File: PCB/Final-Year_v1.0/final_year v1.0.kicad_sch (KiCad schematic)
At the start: 37 parts, among them J1 Power In, J2 Screw_Terminal_01x07, J3 Screw_Terminal_01x03, J4 Screw_Terminal_01x04, J5 Screw_Terminal_01x03, J6 PT1000, J7 HCPV 22x, J8 LDR_module, J9 Screw_Terminal_01x03, U1 LM7805_TO220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

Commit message: added libraries
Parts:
- added BZ1: Buzzer, Buzzer:Buzzer_12x9.5RM7.6, symbol Device:Buzzer
- added C6: 100nF, Capacitor_THT:C_Disc_D6.0mm_W2.5mm_P5.00mm, symbol Device:C
- added C7: 10nF, Capacitor_SMD_2:C_0201_0603Metric, symbol Device:C
- added C8: 0.1uF, Capacitor_THT:C_Disc_D6.0mm_W2.5mm_P5.00mm, symbol Device:C
- added D1: CQY99, LED_THT:LED_D5.0mm_IRGrey, symbol LED:CQY99
- added Q1: 2N3904, Package_TO_SOT_THT:TO-92_Inline, symbol Transistor_BJT:2N3904
- added R19: 1k, Resistor_SMD:R_0201_0603Metric, symbol Device:R
- added R20: 1.2k, Resistor_SMD:R_0201_0603Metric, symbol Device:R
- C1, C4, C5: footprint (none) -> Capacitor_THT:C_Disc_D6.0mm_W2.5mm_P5.00mm
- C2, C3: footprint (none) -> Capacitor_SMD_2:C_0201_0603Metric
- J1, J6: footprint (none) -> TerminalBlock_Phoenix:TerminalBlock_Phoenix_MKDS-1,5-2-5.08_1x02_P5.08mm_Horizontal
- J2: footprint (none) -> TerminalBlock_Phoenix:TerminalBlock_Phoenix_MKDS-1,5-7-5.08_1x07_P5.08mm_Horizontal
- J3, J5, J7, J8, J9: footprint (none) -> TerminalBlock_Phoenix:TerminalBlock_Phoenix_MKDS-1,5-3-5.08_1x03_P5.08mm_Horizontal
- J4: footprint (none) -> TerminalBlock_Phoenix:TerminalBlock_Phoenix_MKDS-1,5-4-5.08_1x04_P5.08mm_Horizontal
- R1, R14, R15, R16, R17, R18, R2, R3: footprint (none) -> Resistor_SMD:R_0201_0603Metric
- R10, R11, R12, R13, R4, R5, R6, R7, R8, R9: footprint (none) -> Resistor_THT:R_Axial_DIN0207_L6.3mm_D2.5mm_P10.16mm_Horizontal
- U5: footprint (none) -> Package_DIP:DIP-14_W7.62mm
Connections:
- net +12V: now also BZ1.1 (-)
- net GND: now also C6.1, C7.1, C8.1, D1.1 (K), Q1.1 (E)
- net at J6.2 (Pin_2), R10.2, U5.5 (+): now also C6.2
- net at R7.2, R8.1, U5.3 (+): now also C7.2
- net D33: now reaches U4.22 (D33)
- net D33: now also R20.1
- net D12: now reaches U4.27 (D12)
- net D12: now also R19.1
- net at R16.2, R17.1, U5.12 (+): now also C8.2
- new net: D1.2 (A), R19.2
- new net: BZ1.2 (+), Q1.3 (C)
- new net: Q1.2 (B), R20.2
- no-connect marks 16 -> 14
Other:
- note added: "Buzzer"
- note added: "Converts 0V - 5V to 0V TO 2V readable range"
- note added: "Final year project"
- note added: "LED"
- note added: "power terminals"

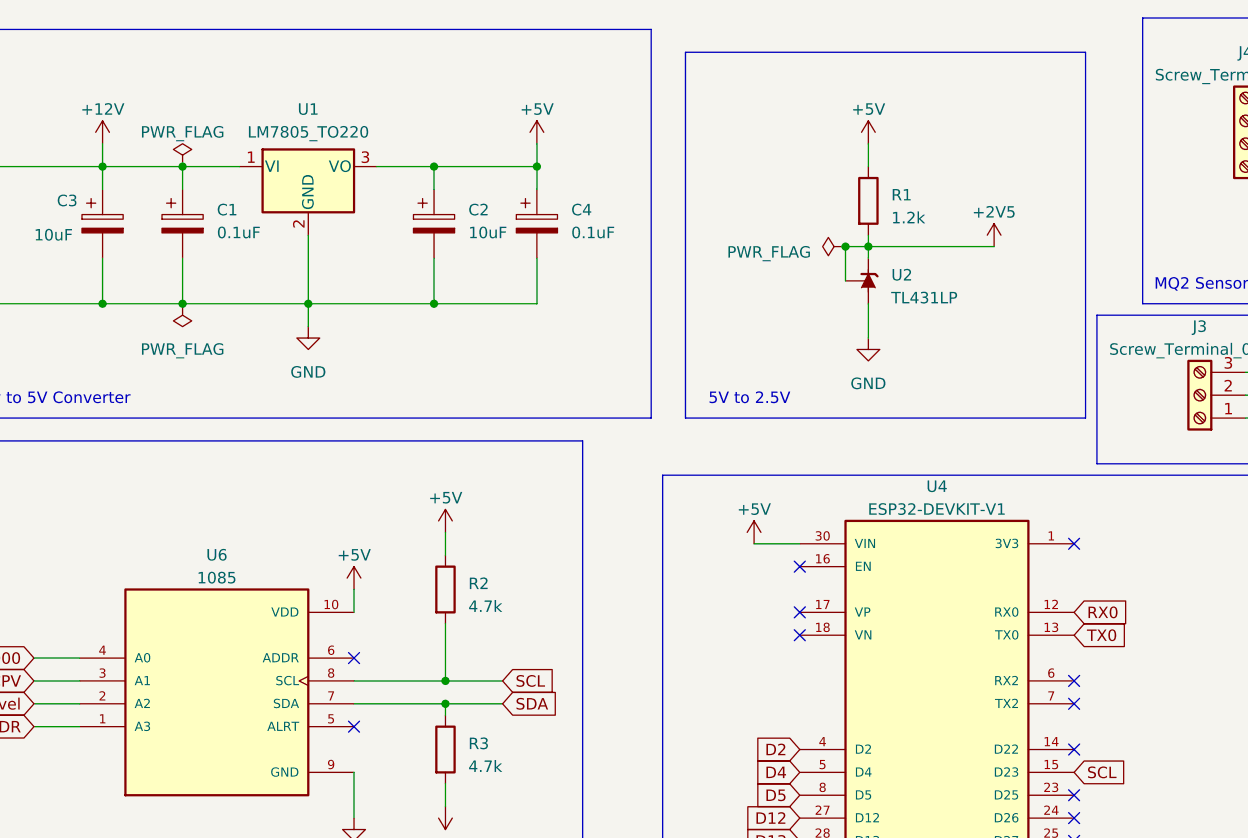
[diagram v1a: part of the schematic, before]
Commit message: address to gnd and decoupling cap to ads
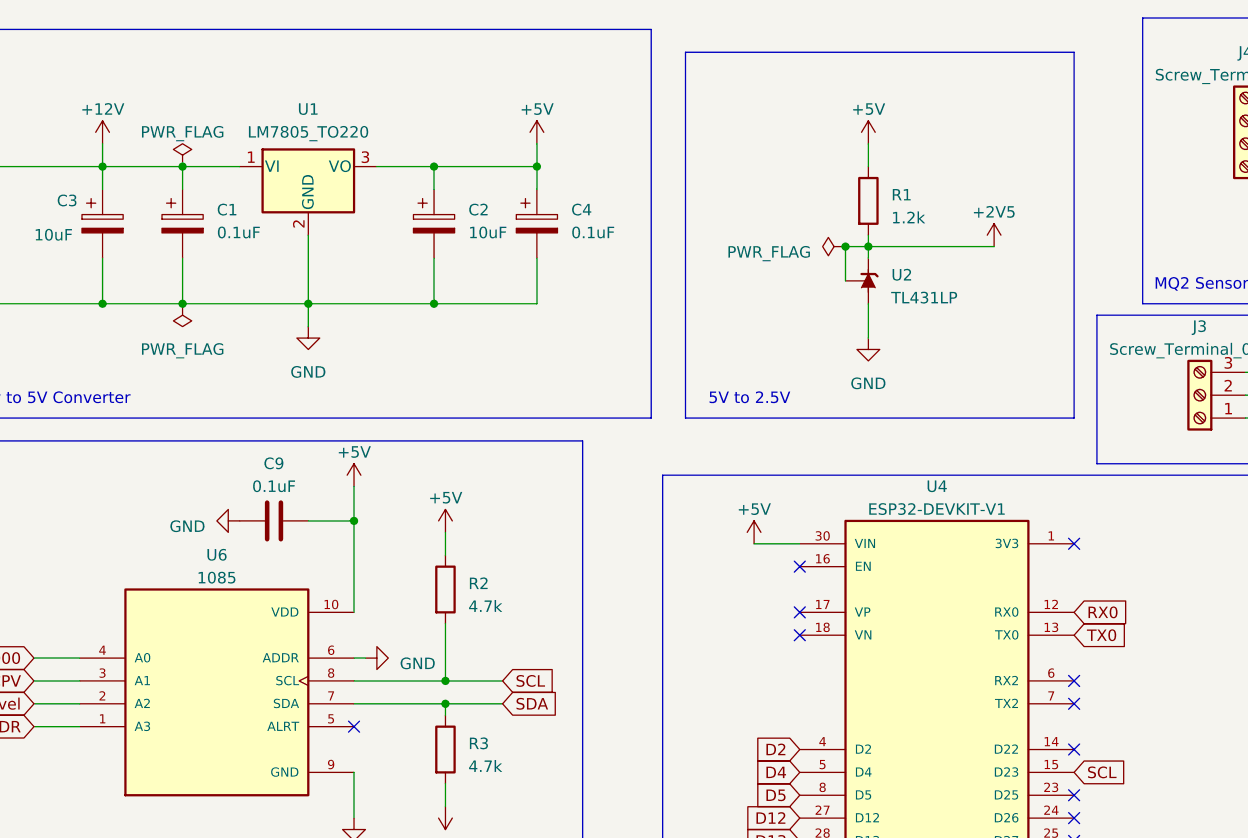
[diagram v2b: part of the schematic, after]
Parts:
- added C9: 0.1uF, Capacitor_THT:C_Disc_D6.0mm_W2.5mm_P5.00mm, symbol Device:C
- BZ1: footprint Buzzer:Buzzer_12x9.5RM7.6 -> Buzzer_Beeper:Buzzer_12x9.5RM7.6
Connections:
- net +5V: now also C9.2
- net GND: now also U6.6 (ADDR), C9.1
- no-connect marks 14 -> 13
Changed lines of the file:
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@@
   (junction (at 43.18 44.45) (diameter 0) (color 0 0 0 0)
+  )
+  (junction (at 71.12 68.58) (diameter 0) (color 0 0 0 0)
   )
   (junction (at 81.28 88.9) (diameter 0) (color 0 0 0 0)
@@
   (no_connect (at 151.13 104.14))
   (no_connect (at 120.65 81.28))
-  (no_connect (at 71.12 83.82))
   (no_connect (at 151.13 111.76))
   (no_connect (at 151.13 88.9))
@@
     (stroke (width 0) (type default))
   )
+  (wire (pts (xy 71.12 68.58) (xy 71.12 78.74))
+    (stroke (width 0) (type default))
+  )
   (wire (pts (xy 240.03 87.63) (xy 220.98 87.63))
     (stroke (width 0) (type default))
@@
     (stroke (width 0) (type default))
   )
+  (wire (pts (xy 66.04 68.58) (xy 71.12 68.58))
+    (stroke (width 0) (type default))
+  )
   (wire (pts (xy 106.68 176.53) (xy 114.3 176.53))
     (stroke (width 0) (type default))
@@
     (stroke (width 0) (type default))
   )
+  (wire (pts (xy 71.12 83.82) (xy 72.39 83.82))
+    (stroke (width 0) (type default))
+  )
   (wire (pts (xy 128.27 142.24) (xy 128.27 144.78))
     (stroke (width 0) (type default))
@@
     (stroke (width 0) (type default))
   )
-  (wire (pts (xy 71.12 76.2) (xy 71.12 78.74))
+  (wire (pts (xy 71.12 64.77) (xy 71.12 68.58))
     (stroke (width 0) (type default))
   )
@@
     (fill (type none))
   )
-  (rectangle (start 107.95 16.51) (end 152.4 57.15)
+  (rectangle (start 107.95 16.51) (end 151.13 57.15)
     (stroke (width 0) (type default))
     (fill (type none))
@@
       (effects (font (size 1.27 1.27)) (justify left))
     )
-    (property "Footprint" "Buzzer:Buzzer_12x9.5RM7.6" (at 319.405 31.75 90)
+    (property "Footprint" "Buzzer_Beeper:Buzzer_12x9.5RM7.6" (at 319.405 31.75 90)
       (effects (font (size 1.27 1.27)) hide)
     )
@@
     )
   )
-  (symbol (lib_id "power:+5V") (at 71.12 76.2 0) (unit 1)
-    (in_bom yes) (on_board yes) (dnp no) (fields_autoplaced)
-    (property "Reference" "#PWR07" (at 71.12 80.01 0)
-      (effects (font (size 1.27 1.27)) hide)
-    )
-    (property "Value" "+5V" (at 71.12 72.39 0)
-      (effects (font (size 1.27 1.27)))
-    )
-    (property "Footprint" "" (at 71.12 76.2 0)
-      (effects (font (size 1.27 1.27)) hide)
-    )
-    (property "Datasheet" "" (at 71.12 76.2 0)
+  (symbol (lib_id "power:+5V") (at 71.12 64.77 0) (unit 1)
+    (in_bom yes) (on_board yes) (dnp no)
+    (property "Reference" "#PWR07" (at 71.12 68.58 0)
+      (effects (font (size 1.27 1.27)) hide)
+    )
+    (property "Value" "+5V" (at 71.12 60.96 0)
+      (effects (font (size 1.27 1.27)))
+    )
+    (property "Footprint" "" (at 71.12 64.77 0)
+      (effects (font (size 1.27 1.27)) hide)
+    )
+    (property "Datasheet" "" (at 71.12 64.77 0)
       (effects (font (size 1.27 1.27)) hide)
     )
@@
     )
   )
+  (symbol (lib_id "power:GND") (at 72.39 83.82 90) (unit 1)
+    (in_bom yes) (on_board yes) (dnp no) (fields_autoplaced)
+    (property "Reference" "#PWR044" (at 78.74 83.82 0)
+      (effects (font (size 1.27 1.27)) hide)
+    )
+    (property "Value" "GND" (at 76.2 84.455 90)
+      (effects (font (size 1.27 1.27)) (justify right))
+    )
+    (property "Footprint" "" (at 72.39 83.82 0)
+      (effects (font (size 1.27 1.27)) hide)
+    )
+    (property "Datasheet" "" (at 72.39 83.82 0)
+      (effects (font (size 1.27 1.27)) hide)
+    )
+    (pin "1")
+    (instances
+      (project "final_year v1.0"
+        (path "/49226e52-308e-4c85-869a-6307490999e3"
+          (reference "#PWR044") (unit 1)
+        )
+      )
+    )
+  )
   (symbol (lib_id "Connector:Screw_Terminal_01x03") (at 165.1 54.61 180) (unit 1)
     (in_bom yes) (on_board yes) (dnp no)
@@
         (path "/49226e52-308e-4c85-869a-6307490999e3"
           (reference "#PWR027") (unit 1)
+        )
+      )
+    )
+  )
+  (symbol (lib_id "Device:C") (at 62.23 68.58 90) (unit 1)
+    (in_bom yes) (on_board yes) (dnp no) (fields_autoplaced)
+    (property "Reference" "C9" (at 62.23 62.23 90)
+      (effects (font (size 1.27 1.27)))
+    )
+    (property "Value" "0.1uF" (at 62.23 64.77 90)
+      (effects (font (size 1.27 1.27)))
+    )
+    (property "Footprint" "Capacitor_THT:C_Disc_D6.0mm_W2.5mm_P5.00mm" (at 66.04 67.6148 0)
+      (effects (font (size 1.27 1.27)) hide)
+    )
+    (property "Datasheet" "~" (at 62.23 68.58 0)
+      (effects (font (size 1.27 1.27)) hide)
+    )
+    (pin "1")
+    (pin "2")
+    (instances
+      (project "final_year v1.0"
+        (path "/49226e52-308e-4c85-869a-6307490999e3"
+          (reference "C9") (unit 1)
         )
       )
@@
         )
       )
+    )
+  )
+  (symbol (lib_id "power:GND") (at 58.42 68.58 270) (unit 1)
+    (in_bom yes) (on_board yes) (dnp no) (fields_autoplaced)
+    (property "Reference" "#PWR045" (at 52.07 68.58 0)
+      (effects (font (size 1.27 1.27)) hide)
+    )
+    (property "Value" "GND" (at 54.61 69.215 90)
+      (effects (font (size 1.27 1.27)) (justify right))
+    )
+    (property "Footprint" "" (at 58.42 68.58 0)
+      (effects (font (size 1.27 1.27)) hide)
+    )
+    (property "Datasheet" "" (at 58.42 68.58 0)
+      (effects (font (size 1.27 1.27)) hide)
+    )
+    (pin "1")
+    (instances
+      (project "final_year v1.0"
+        (path "/49226e52-308e-4c85-869a-6307490999e3"
+          (reference "#PWR045") (unit 1)
+        )
+      )
